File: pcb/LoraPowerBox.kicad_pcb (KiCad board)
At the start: 4 copper layers, 51.6 x 61.1 mm, 48 parts, among them J1 Conn_01x04_Pin, J10 Conn_01x02_Pin, J11 Conn_01x02_Pin, J12 Conn_01x05_Pin, J2 Conn_01x04_Pin, J3 Conn_01x04_Pin, J4 Conn_01x06_Pin, J5 Conn_01x04_Pin, J6 Conn_01x04_Pin, J7 Conn_01x04_Pin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

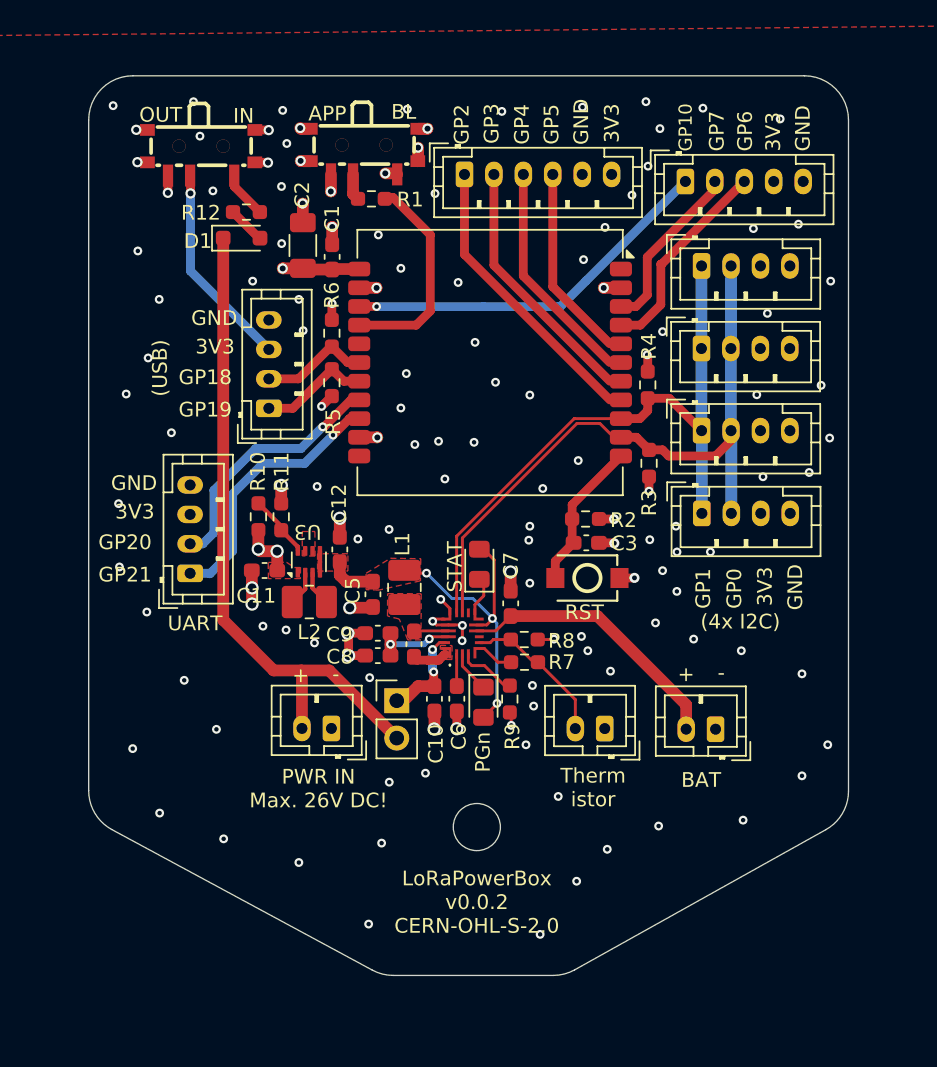
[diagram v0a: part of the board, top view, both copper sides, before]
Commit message: pcb: non-functional clean ups
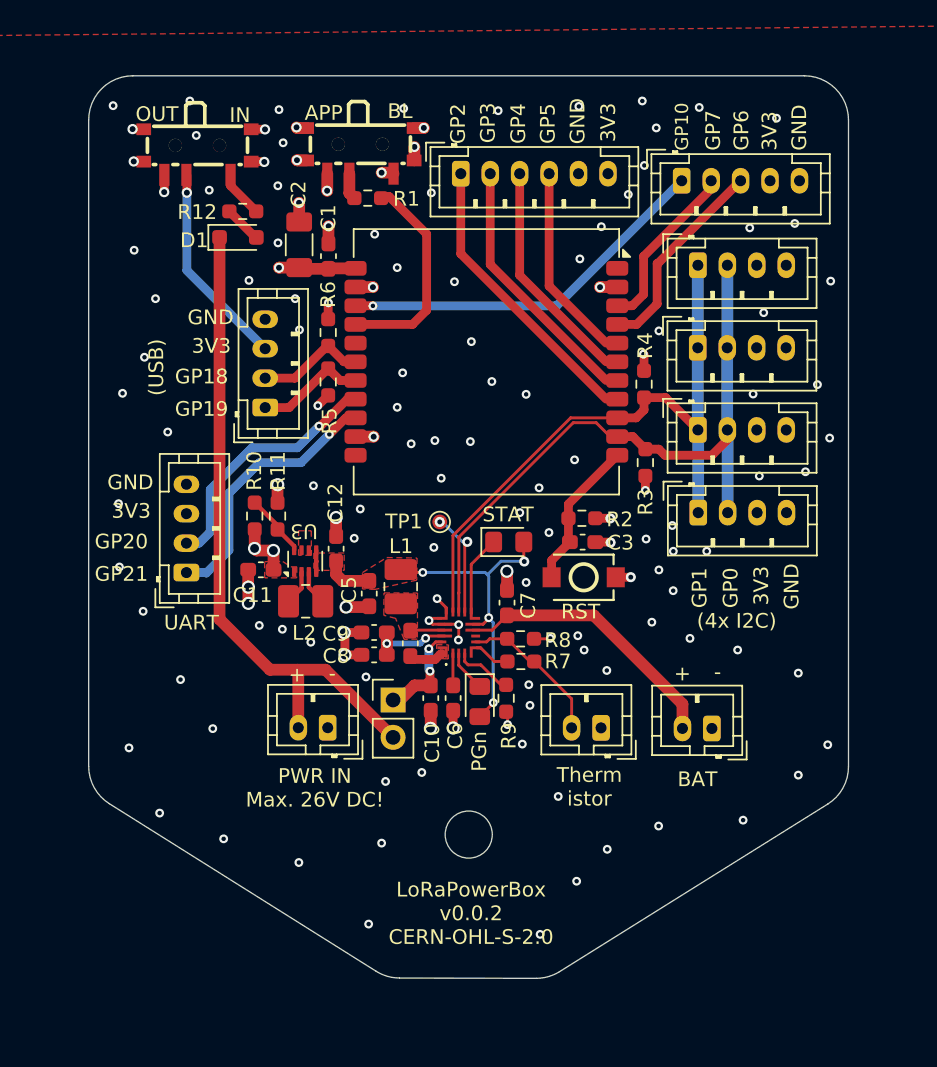
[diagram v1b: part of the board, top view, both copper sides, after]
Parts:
- added TP1: TestPoint, TestPoint:TestPoint_Pad_D1.0mm, F.Cu at (135.8, 69.7)
- moved D2 2.51 mm to (140.5, 71.1), turned to 0 degrees
- moved H1 0.75 mm to (137.8, 90.9)
- moved J1 0.25 mm to (118.6, 73.1)
- moved R8 0.25 mm to (141.3, 77.6)
- moved U3 0.25 mm to (126.7, 72.4)
- moved J12 0.25 mm to (152.2, 46.5)
- moved J6 0.25 mm to (153.3, 63.4)
- moved R1 0.25 mm to (130.9, 47.7)
- moved R4 0.25 mm to (149.7, 60.3)
- moved C1 0.25 mm to (128.2, 51.6)
- moved C10 0.25 mm to (135.2, 81.7)
- moved C11 0.25 mm to (123.6, 72.9)
- moved C12 0.25 mm to (128.8, 71.5)
- moved C2 0.25 mm to (126.2, 50.9)
- moved C3 0.25 mm to (145.5, 71.1)
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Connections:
- U2 pad 11: unconnected-(U2-INTn-Pad11) -> Net-(U2-INTn)
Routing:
- net Net-(U2-INTn): track 0.00 -> 7.28 mm, vias 0 -> 2
- net Net-(D2-K): track 2.61 -> 5.51 mm
- net /SYS: track 25.4 -> 26.3 mm, vias 3 -> 4
- net GND: vias 131 -> 132
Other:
- board size 51.6 x 61.1 mm -> 51.6 x 61.3 mm

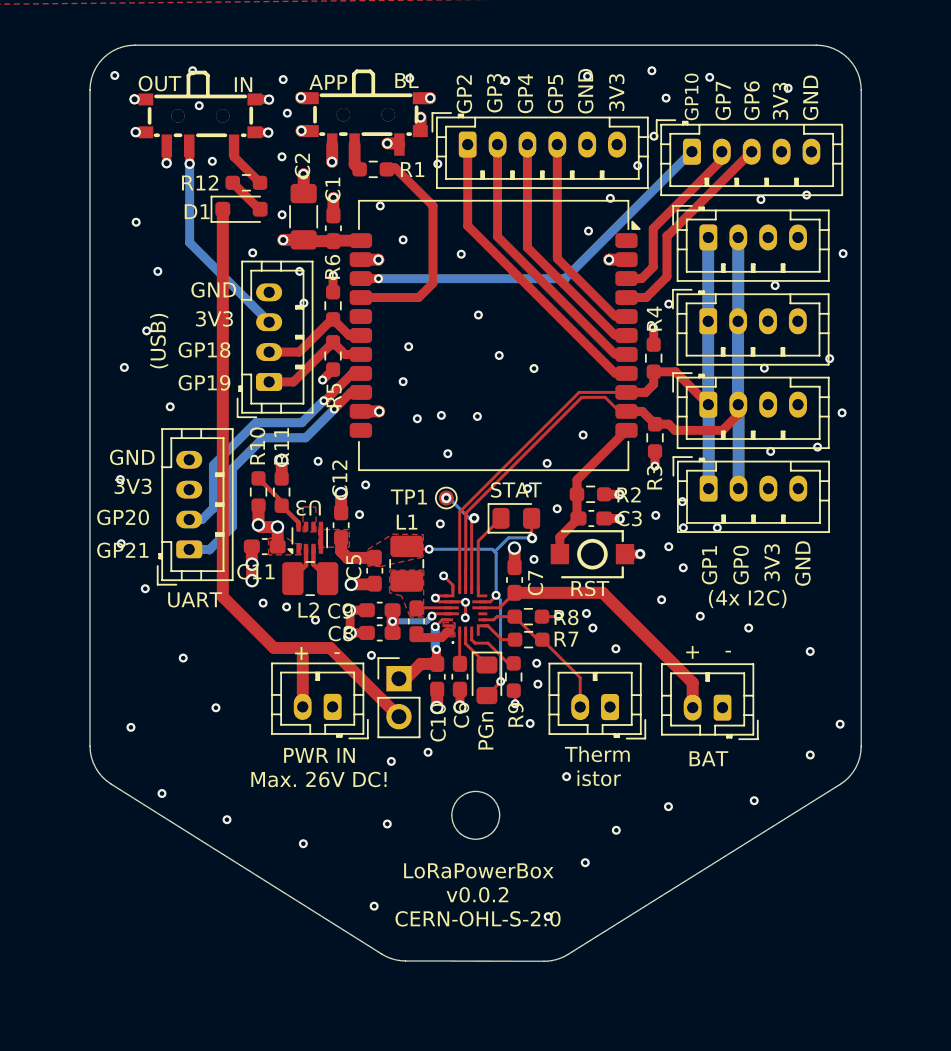
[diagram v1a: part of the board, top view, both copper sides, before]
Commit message: pcb: fix another symmetry issue
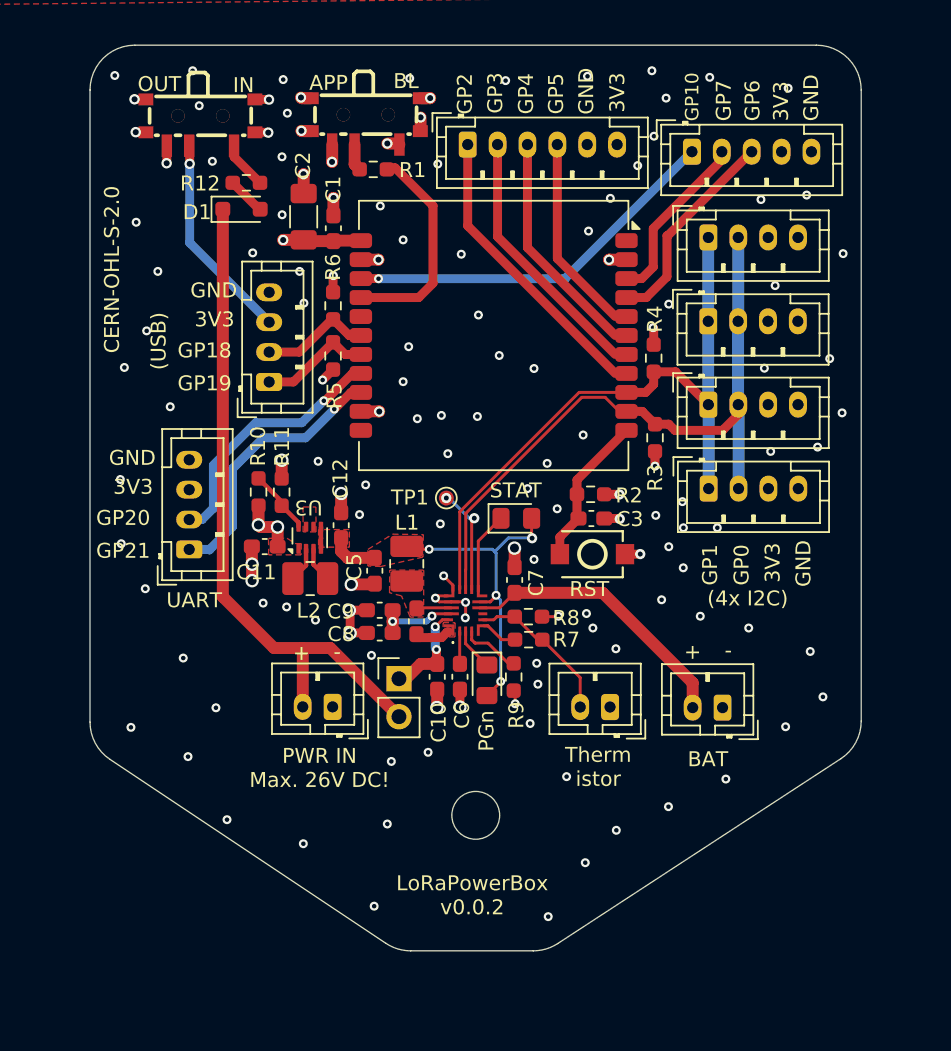
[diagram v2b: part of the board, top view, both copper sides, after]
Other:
- board size 51.6 x 61.3 mm -> 51.6 x 60.6 mm
- board text added: "CERN-OHL-S-2.0"
- board text added: "LoRaPowerBox v0.0.2"
- board text removed: "LoRaPowerBox v0.0.2 CERN-OHL-S-2.0"
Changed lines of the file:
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@@
+	)
+	(gr_line
+		(start 143.247437 99.512001)
+		(end 162.200077 87.137889)
+		(stroke
+			(width 0.0381)
+			(type default)
+		)
+		(layer "Edge.Cuts")
+	)
+	(gr_arc
+		(start 143.247437 99.512001)
+		(mid 142.462928 99.875403)
+		(end 141.60736 100)
+		(stroke
+			(width 0.0381)
+			(type default)
+		)
+		(layer "Edge.Cuts")
 	)
 	(gr_line
@@
 		(layer "Edge.Cuts")
 	)
+	(gr_arc
+		(start 113.275749 87.18216)
+		(mid 112.294933 86.101603)
+		(end 111.94 84.686109)
+		(stroke
+			(width 0.0381)
+			(type default)
+		)
+		(layer "Edge.Cuts")
+	)
 	(gr_line
-		(start 163.56 86.315697)
+		(start 163.56 84.625888)
 		(end 163.56 42.38)
 		(stroke
@@
 	)
 	(gr_arc
-		(start 113.344366 88.832007)
-		(mid 112.314445 87.742943)
-		(end 111.94 86.291544)
+		(start 163.56 84.625888)
+		(mid 163.198203 86.054133)
+		(end 162.200077 87.137889)
 		(stroke
 			(width 0.05)
+			(type default)
+		)
+		(layer "Edge.Cuts")
+	)
+	(gr_line
+		(start 133.408426 100)
+		(end 141.60736 100)
+		(stroke
+			(width 0.0381)
 			(type default)
 		)
@@
 	(gr_line
 		(start 111.94 42.38)
-		(end 111.94 86.291544)
+		(end 111.94 84.686109)
 		(stroke
 			(width 0.05)
@@
 	)
 	(gr_line
-		(start 143.932618 100.242247)
-		(end 162.149665 88.8599)
+		(start 131.744175 99.496051)
+		(end 113.275749 87.18216)
 		(stroke
 			(width 0.0381)
-			(type default)
-		)
-		(layer "Edge.Cuts")
-	)
-	(gr_arc
-		(start 163.56 86.315697)
-		(mid 163.183834 87.770175)
-		(end 162.149665 88.8599)
-		(stroke
-			(width 0.0381)
-			(type default)
-		)
-		(layer "Edge.Cuts")
-	)
-	(gr_arc
-		(start 133.060297 100.676955)
-		(mid 132.233595 100.558845)
-		(end 131.471481 100.217426)
-		(stroke
-			(width 0.05)
-			(type default)
-		)
-		(layer "Edge.Cuts")
-	)
-	(gr_line
-		(start 133.060297 100.676955)
-		(end 142.336135 100.698037)
-		(stroke
-			(width 0.05)
-			(type default)
-		)
-		(layer "Edge.Cuts")
-	)
-	(gr_arc
-		(start 143.932618 100.242247)
-		(mid 143.166535 100.582777)
-		(end 142.336135 100.698037)
-		(stroke
-			(width 0.05)
 			(type default)
 		)
@@
 		(layer "Edge.Cuts")
 	)
-	(gr_line
-		(start 131.471481 100.217426)
-		(end 113.344366 88.832007)
+	(gr_arc
+		(start 133.408426 100)
+		(mid 132.538984 99.871257)
+		(end 131.744175 99.496051)
 		(stroke
 			(width 0.0381)
@@
 		)
 	)
+	(gr_text "CERN-OHL-S-2.0"
+		(at 114 60 90)
+		(layer "F.SilkS")
+		(effects
+			(font
+				(size 1 1)
+				(thickness 0.125)
+			)
+			(justify left bottom)
+		)
+	)
 	(gr_text "PWR IN\nMax. 26V DC!"
 		(at 127.3 89.15125 0)
@@
 		)
 	)
-	(gr_text "LoRaPowerBox\nv0.0.2\nCERN-OHL-S-2.0\n"
-		(at 137.92 98.48 0)
-		(layer "F.SilkS")
-		(effects
-			(font
-				(size 1 1)
-				(thickness 0.1875)
+	(gr_text "LoRaPowerBox\nv0.0.2\n"
+		(at 137.525 97.675 0)
+		(layer "F.SilkS")
+		(effects
+			(font
+				(size 1 1)
+				(thickness 0.125)
 			)
 			(justify bottom)
@@
 	)
 	(via
-		(at 162.15 84.83)
+		(at 161 83)
 		(size 0.6)
 		(drill 0.3)
@@
 	)
 	(via
-		(at 160.15 86.89125)
+		(at 158.5 85)
 		(size 0.6)
 		(drill 0.3)
@@
 	)
 	(via
-		(at 116.76 89.47)
+		(at 118.5 87)
 		(size 0.6)
 		(drill 0.3)
@@
 	)
 	(via
-		(at 156.4 89.95)
-		(size 0.6)
-		(drill 0.3)
+		(at 154.5 88.5)
+		(size 0.6)
+		(drill 0.3)

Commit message: pcb: add a few more vias to gnd
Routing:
- net GND: vias 132 -> 136
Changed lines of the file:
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@@
+	)
+	(via
+		(at 149.525 83)
+		(size 0.6858)
+		(drill 0.3302)
+		(layers "F.Cu" "B.Cu")
+		(free yes)
+		(net 1)
 	)
 	(via
@@
 		(size 0.6)
 		(drill 0.3)
+		(layers "F.Cu" "B.Cu")
+		(free yes)
+		(net 1)
+	)
+	(via
+		(at 157.6 74.1)
+		(size 0.6858)
+		(drill 0.3302)
 		(layers "F.Cu" "B.Cu")
 		(free yes)
@@
 	)
 	(via
+		(at 149.325 87.15)
+		(size 0.6858)
+		(drill 0.3302)
+		(layers "F.Cu" "B.Cu")
+		(free yes)
+		(net 1)
+	)
+	(via
 		(at 114.03 72.75)
 		(size 0.6)
@@
 		(layers "F.Cu" "B.Cu")
 		(free yes)
+		(net 1)
+	)
+	(via
+		(at 145.575 73.3)
+		(size 0.6858)
+		(drill 0.3302)
+		(layers "F.Cu" "B.Cu")
+		(free yes)

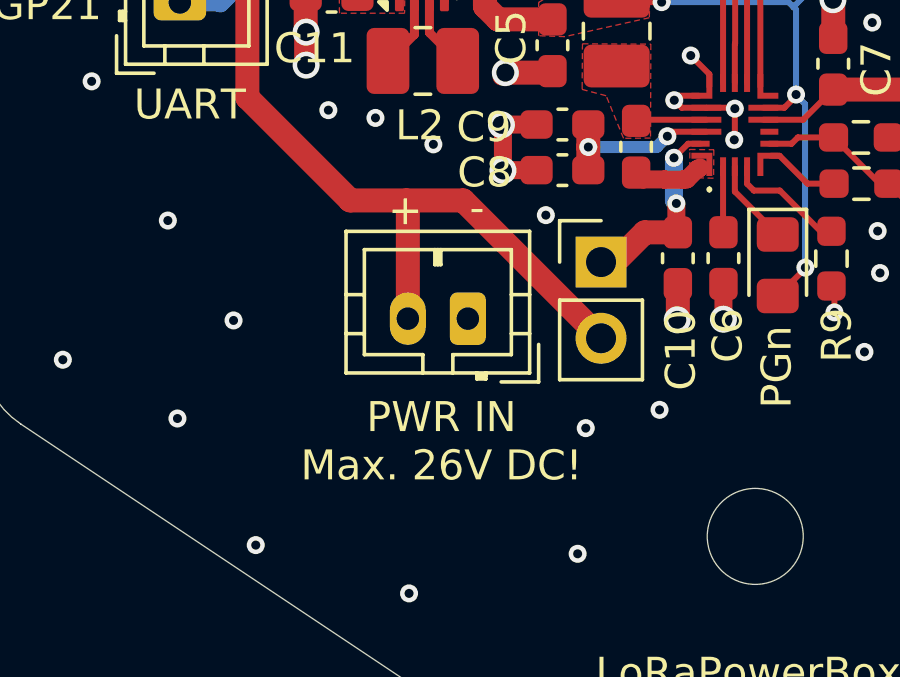
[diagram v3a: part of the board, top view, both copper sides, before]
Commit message: pcb, doc: move PWR IN a little bit to the left
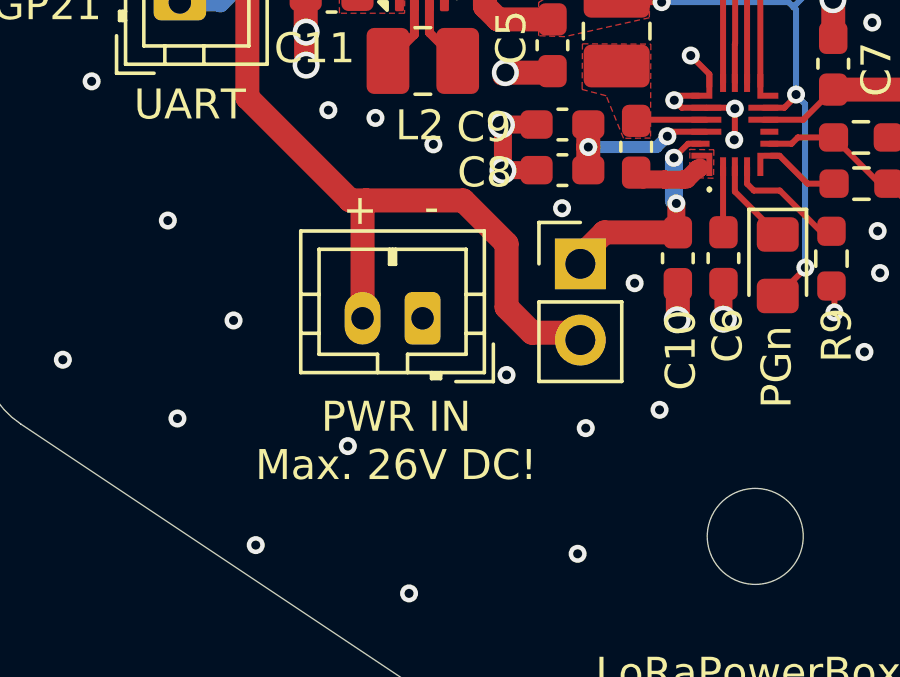
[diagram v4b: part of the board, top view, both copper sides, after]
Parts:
- moved J11 1.51 mm to (126.7, 83.7)
- moved J8 0.69 mm to (131.9, 81.8)
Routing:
- net Net-(J8-Pin_1): track 6.52 -> 7.13 mm
- net GND: vias 136 -> 139
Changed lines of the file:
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@@
 	(footprint "Connector_JST:JST_PH_B2B-PH-K_1x02_P2.00mm_Vertical"
 		(layer "F.Cu")
-		(at 128.18 83.67125 180)
+		(at 126.67 83.66 180)
 		(descr "JST PH series connector, B2B-PH-K (http://www.jst-mfg.com/product/pdf/eng/ePH.pdf), generated with kicad-footprint-generator")
 		(tags "connector JST PH vertical")
@@
 	(footprint "Connector_PinHeader_2.54mm:PinHeader_1x02_P2.54mm_Vertical"
 		(layer "F.Cu")
-		(at 132.62 81.78625)
+		(at 131.93 81.845)
 		(descr "Through hole straight pin header, 1x02, 2.54mm pitch, single row")
 		(tags "Through hole pin header THT 1x02 2.54mm single row")
@@
 	)
 	(gr_text "PWR IN\nMax. 26V DC!"
-		(at 127.3 89.15125 0)
+		(at 125.79 89.14 0)
 		(layer "F.SilkS")
 		(effects
@@
 	)
 	(gr_text "-"
-		(at 128.73 79.57125 180)
+		(at 127.22 79.56 180)
 		(layer "F.SilkS")
 		(effects
@@
 	)
 	(gr_text "+"
-		(at 126.67 79.54125 180)
+		(at 125.16 79.53 180)
 		(layer "F.SilkS")
 		(effects
@@
 	)
 	(via
+		(at 131.32 79.99)
+		(size 0.6)
+		(drill 0.3)
+		(layers "F.Cu" "B.Cu")
+		(free yes)
+		(net 1)
+	)
+	(via
 		(at 147.17 91.93)
 		(size 0.6)
@@
 	)
 	(via
+		(at 129.47 85.55)
+		(size 0.6)
+		(drill 0.3)
+		(layers "F.Cu" "B.Cu")
+		(free yes)
+		(net 1)
+	)
+	(via
 		(at 124.8 50.73125)
 		(size 0.6)
@@
 	)
 	(via
+		(at 133.74 82.49)
+		(size 0.6)
+		(drill 0.3)
+		(layers "F.Cu" "B.Cu")
+		(free yes)
+		(net 1)
+	)
+	(via
 		(at 113.97 68.45)
 		(size 0.6)
@@
 	)
 	(via
+		(at 124.18 87.92)
+		(size 0.6)
+		(drill 0.3)
+		(layers "F.Cu" "B.Cu")
+		(free yes)
+		(net 1)
+	)
+	(via
 		(at 129.35 78.73125)
 		(size 0.9)
@@
 	)
 	(via
-		(at 130.78 80.22125)
-		(size 0.6)
-		(drill 0.3)
-		(layers "F.Cu" "B.Cu")
-		(free yes)
-		(net 1)
-	)
-	(via
 		(at 127.21 67.23125)
 		(size 0.6)
@@
 	)
 	(segment
-		(start 126.18 79.78125)
-		(end 126.13 79.73125)
-		(width 0.6)
+		(start 128.025 79.73125)
+		(end 129.47 81.17625)
+		(width 0.8)
 		(layer "F.Cu")
 		(net 8)
 	)
 	(segment
-		(start 126.18 83.67125)
-		(end 126.18 79.78125)
+		(start 120.83 50.36125)
+		(end 120.83 76.30125)
 		(width 0.8)
 		(layer "F.Cu")
@@
 	)
 	(segment
-		(start 120.83 50.36125)
-		(end 120.83 76.30125)
+		(start 129.47 83.29)
+		(end 130.32 84.14)
+		(width 0.8)
+		(layer "F.Cu")
+		(net 8)
+	)
+	(segment
+		(start 129.47 81.17625)
+		(end 129.47 83.29)
 		(width 0.8)
 		(layer "F.Cu")
@@
 	)
 	(segment
-		(start 128.025 79.73125)
-		(end 126.13 79.73125)
+		(start 130.32 84.14)
+		(end 131.93 84.14)
 		(width 0.8)
 		(layer "F.Cu")
@@
 	)
 	(segment
-		(start 132.62 84.32625)
-		(end 128.025 79.73125)
+		(start 124.67 79.85125)
+		(end 124.67 83.66)
 		(width 0.8)
 		(layer "F.Cu")
@@
 	)
 	(segment
-		(start 126.13 79.73125)
+		(start 124.79 79.73125)
 		(end 124.26 79.73125)
 		(width 0.8)
@@
 	)
 	(segment
-		(start 133.085 81.78625)
-		(end 134.075 80.79625)
+		(start 124.79 79.73125)
+		(end 124.67 79.85125)
 		(width 0.8)
 		(layer "F.Cu")
-		(net 9)
+		(net 8)
+	)
+	(segment
+		(start 124.79 79.73125)
+		(end 128.025 79.73125)
+		(width 0.8)
+		(layer "F.Cu")
+		(net 8)
 	)
 	(segment
@@
 	)
 	(segment
-		(start 132.62 81.78625)
-		(end 133.085 81.78625)
+		(start 132.73375 80.79625)
+		(end 131.93 81.6)
 		(width 0.8)
 		(layer "F.Cu")
@@
 	)
 	(segment
-		(start 134.075 80.79625)
-		(end 135.18 80.79625)
+		(start 135.18 80.79625)
+		(end 132.73375 80.79625)
 		(width 0.8)
 		(layer "F.Cu")
